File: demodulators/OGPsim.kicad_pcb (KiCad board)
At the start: 4 copper layers, 35 x 9.7 mm, 39 parts, among them J1 Conn_01x02, J2 Conn_01x02, J3 Conn_01x02, J4 Conn_01x02, J5 Conn_01x02, U2 AD8668ARZ-ND

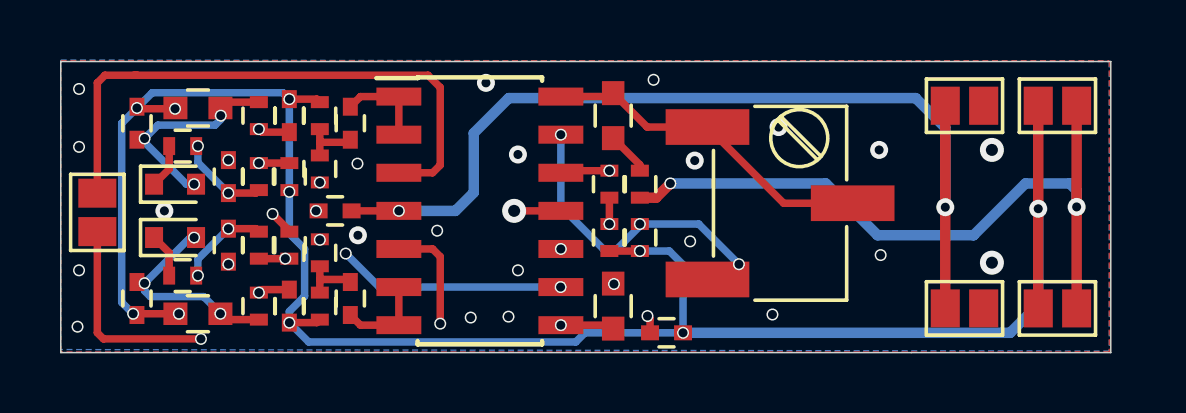
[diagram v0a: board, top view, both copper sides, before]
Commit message: Added name and date to silkscreen on all boards. Sending design to PCB fab house tonight!
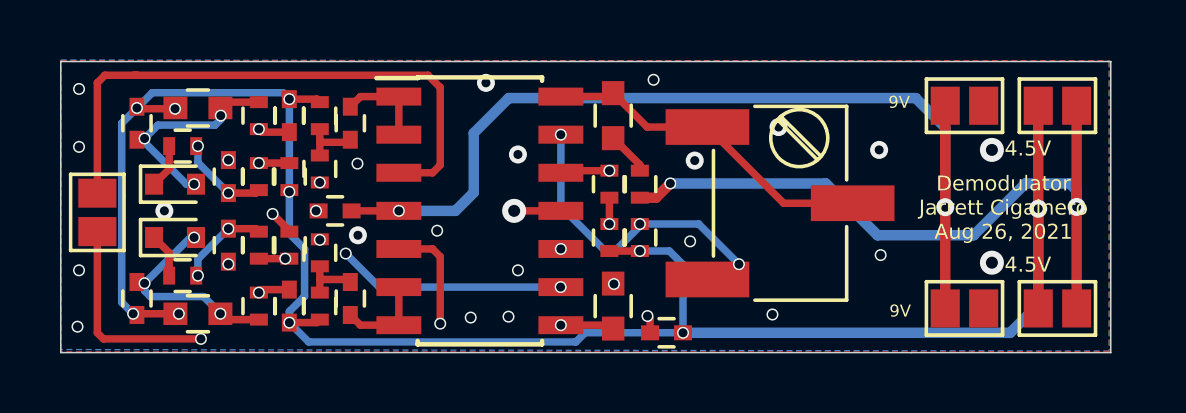
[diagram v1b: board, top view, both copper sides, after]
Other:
- board text added: "4.5V"
- board text added: "9V"
- board text added: "Demodulator Jarrett Cigainero Aug 26, 2021"
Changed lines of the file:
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@@
   (general
     (thickness 1.6)
-    (drawings 11)
+    (drawings 16)
     (tracks 289)
     (zones 0)
@@
       (net 2 +9V))
   )
+  (gr_text 4.5V (at 164.77488 104.00284) (layer F.SilkS)
+    (effects (font (size 0.5 0.5) (thickness 0.125)))
+  )
+  (gr_text 4.5V (at 164.77488 100.13188) (layer F.SilkS)
+    (effects (font (size 0.5 0.5) (thickness 0.125)))
+  )
+  (gr_text "9V\n" (at 160.51784 105.54716) (layer F.SilkS)
+    (effects (font (size 0.4 0.4) (thickness 0.1)))
+  )
+  (gr_text "9V\n" (at 160.48228 98.58756) (layer F.SilkS)
+    (effects (font (size 0.4 0.4) (thickness 0.1)))
+  )
+  (gr_text "Demodulator\nJarrett Cigainero\nAug 26, 2021" (at 163.96208 102.10292) (layer F.SilkS)
+    (effects (font (size 0.5 0.5) (thickness 0.125)))
+  )
   (gr_line (start 143.56588 97.53092) (end 142.79372 98.36912) (layer Dwgs.User) (width 0.15))
